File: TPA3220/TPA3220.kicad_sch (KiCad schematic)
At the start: 0 parts

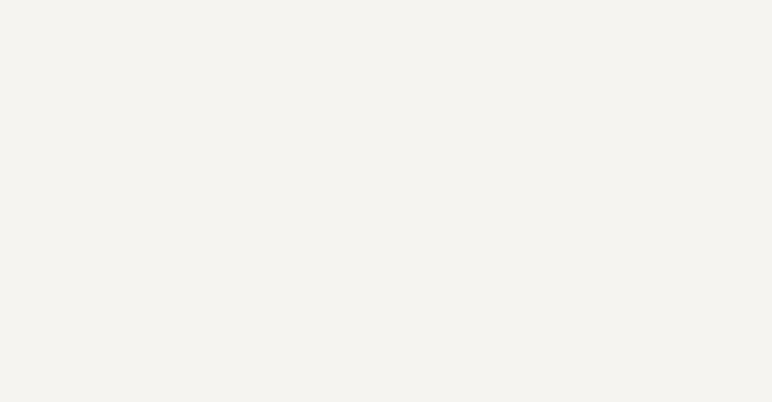
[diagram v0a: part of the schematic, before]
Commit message: TPA3220: snapshot before agent schematic completion
Co-Authored-By: Claude Opus 5.5 <noreply@anthropic.com>
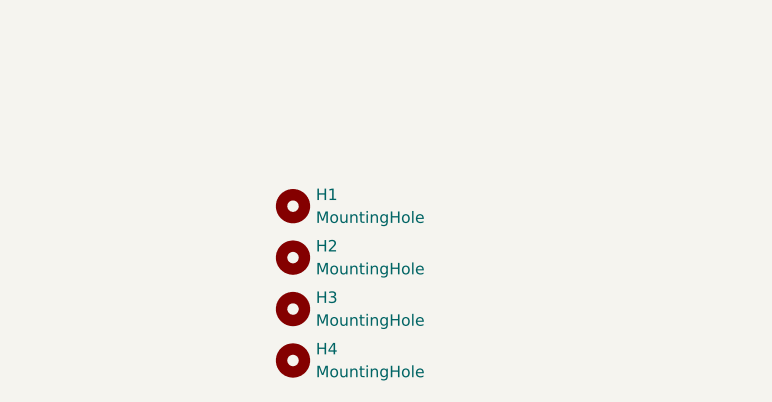
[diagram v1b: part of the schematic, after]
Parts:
- added H1, H2, H3, H4: MountingHole, MountingHole:MountingHole_3.2mm_M3, symbol Mechanical:MountingHole
